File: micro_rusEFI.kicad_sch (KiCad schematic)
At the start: 22 parts, among them U3 molex_48pin_MRE

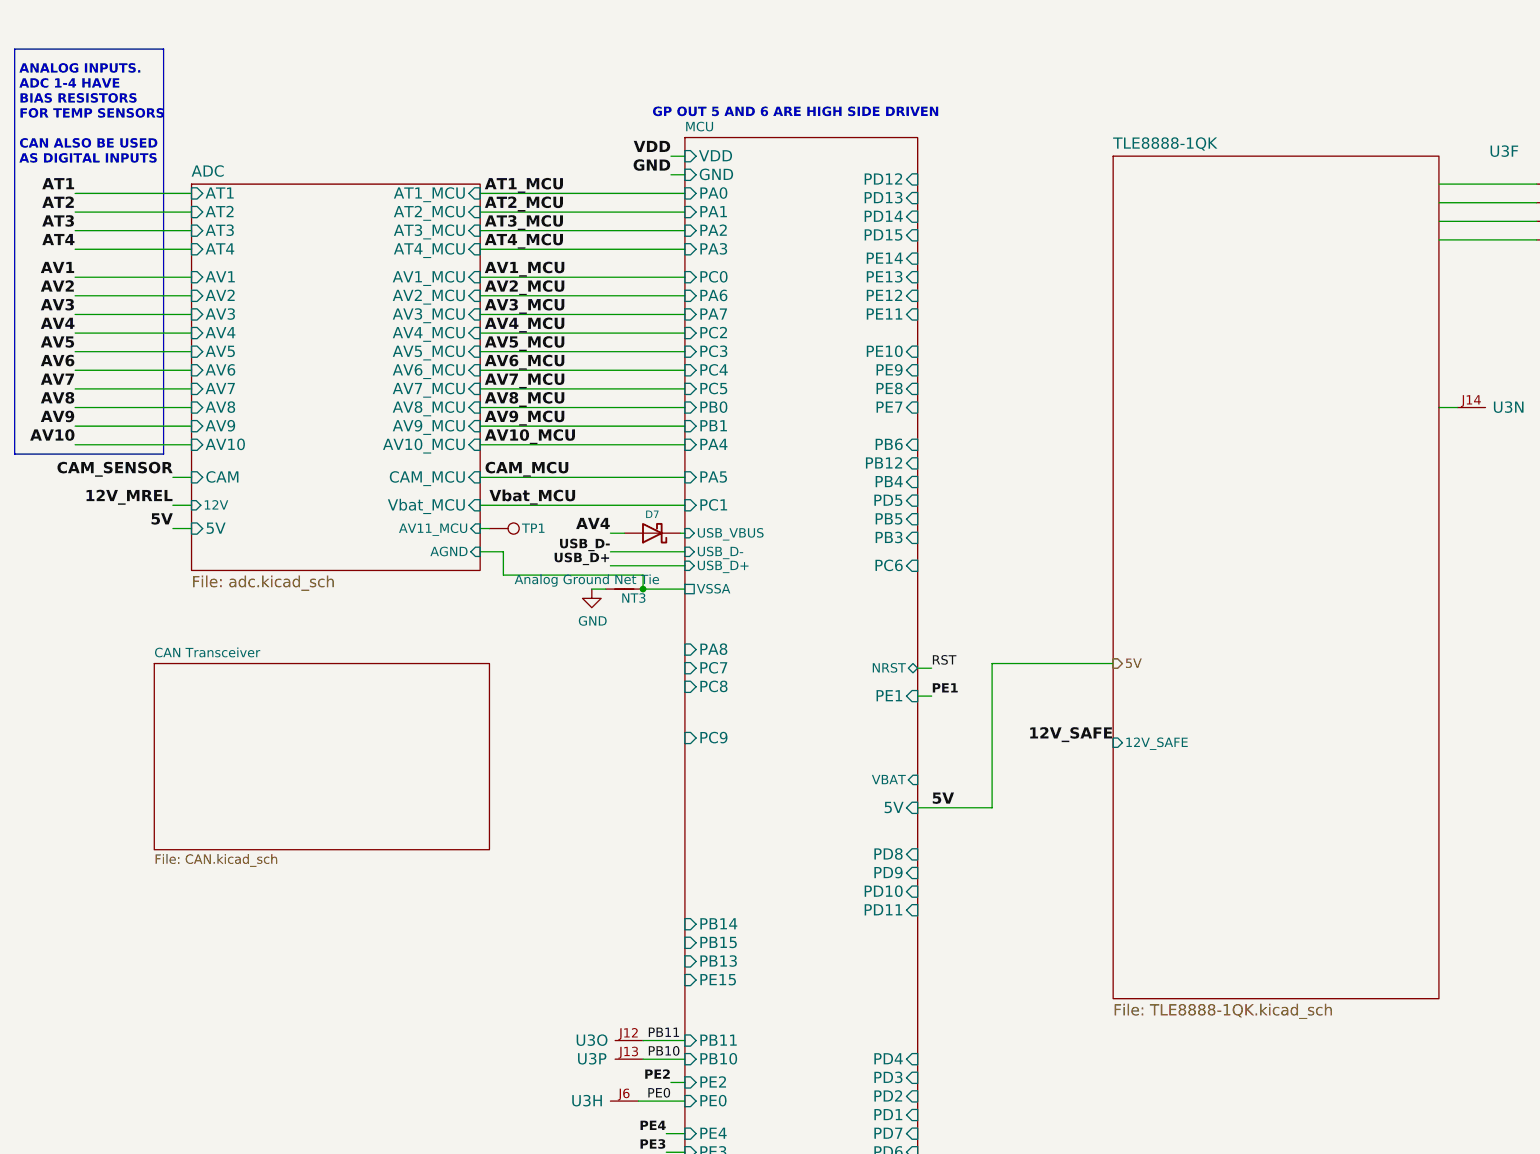
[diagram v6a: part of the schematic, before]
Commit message: Fixed CAN and 5v pads
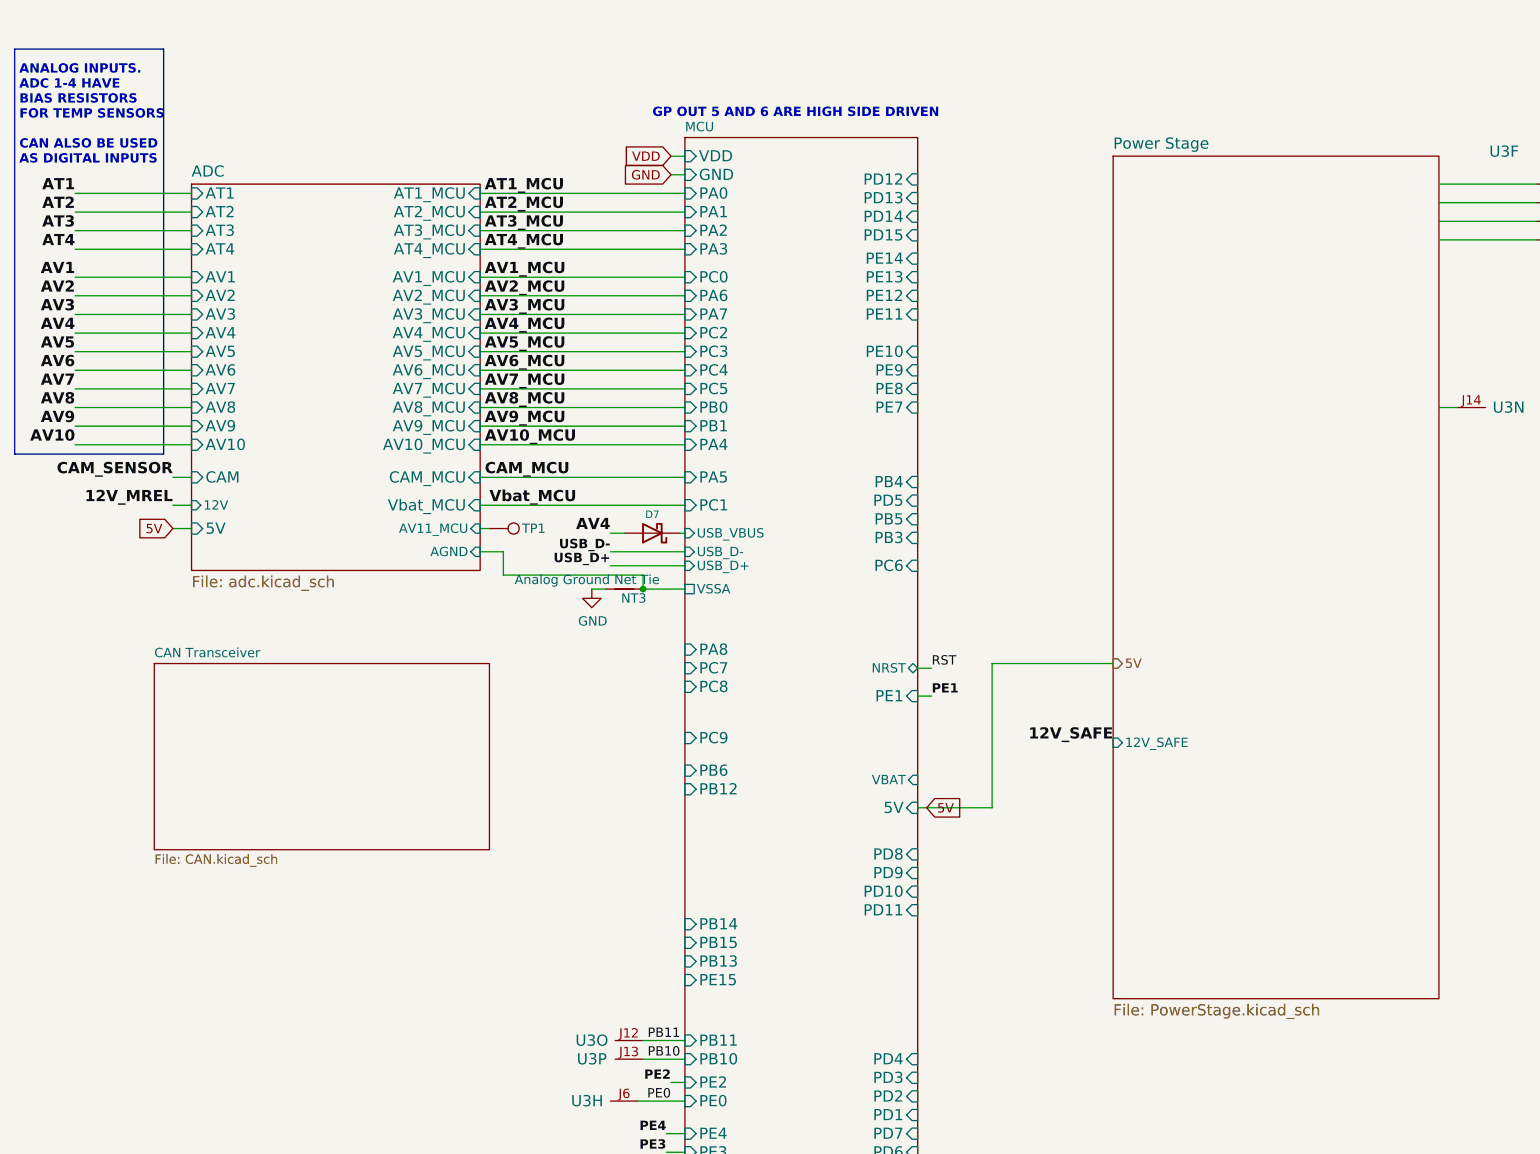
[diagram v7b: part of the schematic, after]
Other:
- sheet TLE8888-1QK renamed Power Stage
- sheet Power Stage: file TLE8888-1QK.kicad_sch -> PowerStage.kicad_sch
- title: microRusEFI-2L -> MRE IO Expander
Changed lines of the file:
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@@
   (paper "B")
   (title_block
-    (title "microRusEFI-2L")
-    (date "2020-05-24")
-    (rev "R0.5.2")
+    (title "MRE IO Expander")
+    (date "2021-02-")
+    (rev "R0.1")
     (company "rusEFI.com")
-    (comment 1 "Donald Becker")
+    (comment 1 "Simon Orchard")
     (comment 2 "AI6OD")
   )
@@
     (effects (font (size 1.27 1.27) (thickness 0.254) bold) (justify right bottom))
   )
-  (label "5V" (at 203.835 172.085 0)
-    (effects (font (size 1.524 1.524) (thickness 0.3048) bold) (justify left bottom))
-  )
-  (label "VDD" (at 168.275 83.185 180)
-    (effects (font (size 1.524 1.524) (thickness 0.3048) bold) (justify right bottom))
-  )
   (label "AT3" (at 184.15 41.91 270)
     (effects (font (size 1.524 1.524) (thickness 0.3048) bold) (justify right bottom))
@@
     (effects (font (size 1.27 1.27) (thickness 0.254) bold) (justify right bottom))
   )
-  (label "5V" (at 100.33 133.985 180)
-    (effects (font (size 1.524 1.524) (thickness 0.3048) bold) (justify right bottom))
-  )
   (label "PC10" (at 167.64 234.315 180)
     (effects (font (size 1.27 1.27)) (justify right bottom))
@@
     (effects (font (size 1.524 1.524) (thickness 0.3048) bold) (justify right bottom))
   )
-  (label "GND" (at 168.275 85.725 180)
-    (effects (font (size 1.524 1.524) (thickness 0.3048) bold) (justify right bottom))
-  )
   (label "CANL" (at 248.92 41.91 270)
     (effects (font (size 1.524 1.524) (thickness 0.3048) bold) (justify right bottom))
@@
   (label "AT1" (at 86.995 88.265 180)
     (effects (font (size 1.524 1.524) (thickness 0.3048) bold) (justify right bottom))
+  )
+  (global_label "5V" (shape input) (at 203.1526 172.085 0) (fields_autoplaced)
+    (effects (font (size 1.27 1.27)) (justify left))
+    (property "Intersheet References" "${INTERSHEET_REFS}" (id 0) (at 207.7749 172.0056 0)
+      (effects (font (size 1.27 1.27)) (justify left) hide)
+    )
+  )
+  (global_label "5V" (shape input) (at 100.33 133.985 180) (fields_autoplaced)
+    (effects (font (size 1.27 1.27)) (justify right))
+    (property "Intersheet References" "${INTERSHEET_REFS}" (id 0) (at 95.7077 133.9056 0)
+      (effects (font (size 1.27 1.27)) (justify right) hide)
+    )
+  )
+  (global_label "GND" (shape input) (at 168.275 85.725 180) (fields_autoplaced)
+    (effects (font (size 1.27 1.27)) (justify right))
+    (property "Intersheet References" "${INTERSHEET_REFS}" (id 0) (at 162.0803 85.6456 0)
+      (effects (font (size 1.27 1.27)) (justify right) hide)
+    )
+  )
+  (global_label "VDD" (shape input) (at 168.275 83.185 180) (fields_autoplaced)
+    (effects (font (size 1.27 1.27)) (justify right))
+    (property "Intersheet References" "${INTERSHEET_REFS}" (id 0) (at 162.3222 83.1056 0)
+      (effects (font (size 1.27 1.27)) (justify right) hide)
+    )
   )
   (hierarchical_label "5V" (shape output) (at 228.6 152.4 0)
@@
     (stroke (width 0) (type solid) (color 0 0 0 0))
     (fill (color 0 0 0 0.0000))
-    (property "Sheet name" "TLE8888-1QK" (id 0) (at 228.6 82.3464 0)
+    (property "Sheet name" "Power Stage" (id 0) (at 228.6 82.3464 0)
       (effects (font (size 1.524 1.524)) (justify left bottom))
     )
-    (property "Sheet file" "TLE8888-1QK.kicad_sch" (id 1) (at 228.6 198.8062 0)
+    (property "Sheet file" "PowerStage.kicad_sch" (id 1) (at 228.6 198.8062 0)
       (effects (font (size 1.524 1.524)) (justify left top))
     )
@@
       (effects (font (size 1.524 1.524)) (justify left))
     )
-    (pin "PB12" input (at 201.93 125.095 0)
-      (effects (font (size 1.524 1.524)) (justify right))
+    (pin "PB12" input (at 170.18 169.545 180)
+      (effects (font (size 1.524 1.524)) (justify left))
     )
     (pin "PB14" input (at 170.18 187.96 180)
@@
       (effects (font (size 1.524 1.524)) (justify left))
     )
-    (pin "PB6" input (at 201.93 122.555 0)
-      (effects (font (size 1.524 1.524)) (justify right))
+    (pin "PB6" input (at 170.18 167.005 180)
+      (effects (font (size 1.524 1.524)) (justify left))
     )
     (pin "PB4" input (at 201.93 127.635 0)

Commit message: Fixing tags
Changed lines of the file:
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@@
     (effects (font (size 1.524 1.524) (thickness 0.3048) bold) (justify right bottom))
   )
-  (global_label "5V" (shape input) (at 203.1526 172.085 0) (fields_autoplaced)
+  (global_label "5V" (shape input) (at 212.09 172.085 0) (fields_autoplaced)
     (effects (font (size 1.27 1.27)) (justify left))
-    (property "Intersheet References" "${INTERSHEET_REFS}" (id 0) (at 207.7749 172.0056 0)
+    (property "Intersheet References" "${INTERSHEET_REFS}" (id 0) (at 216.7123 172.0056 0)
       (effects (font (size 1.27 1.27)) (justify left) hide)
     )
